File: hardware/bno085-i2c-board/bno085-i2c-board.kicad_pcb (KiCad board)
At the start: 2 copper layers, 9.5 x 15.5 mm, 8 parts, among them J1 Conn_01x06_Pin

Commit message: pcb
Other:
- board size 9.5 x 15.5 mm -> 9.5 x 15 mm
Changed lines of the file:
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@@
   (gr_arc (start 163.5 97) (mid 163.353553 97.353553) (end 163 97.5)
     (stroke (width 0.1) (type default)) (layer "Edge.Cuts"))
-  (gr_arc (start 163 82) (mid 163.353553 82.146447) (end 163.5 82.5)
+  (gr_arc (start 163 82.5) (mid 163.353553 82.646447) (end 163.5 83)
     (stroke (width 0.1) (type default)) (layer "Edge.Cuts"))
-  (gr_line (start 154 82.5) (end 154 97)
+  (gr_line (start 154 83) (end 154 97)
     (stroke (width 0.1) (type default)) (layer "Edge.Cuts"))
   (gr_arc (start 154.5 97.5) (mid 154.146447 97.353553) (end 154 97)
     (stroke (width 0.1) (type default)) (layer "Edge.Cuts"))
-  (gr_arc (start 154 82.5) (mid 154.146447 82.146447) (end 154.5 82)
+  (gr_arc (start 154 83) (mid 154.146447 82.646447) (end 154.5 82.5)
     (stroke (width 0.1) (type default)) (layer "Edge.Cuts"))
-  (gr_line (start 163 82) (end 154.5 82)
+  (gr_line (start 163 82.5) (end 154.5 82.5)
     (stroke (width 0.1) (type default)) (layer "Edge.Cuts"))
-  (gr_line (start 163.5 82.5) (end 163.5 97)
+  (gr_line (start 163.5 83) (end 163.5 97)
     (stroke (width 0.1) (type default)) (layer "Edge.Cuts"))
   (gr_line (start 163 97.5) (end 154.5 97.5)

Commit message: pcb
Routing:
- net GND: track 24.6 -> 41.8 mm
- net /H_SCL: track 13.1 -> 18.7 mm
- net +3.3V: track 21.9 -> 24.2 mm, vias 2 -> 3

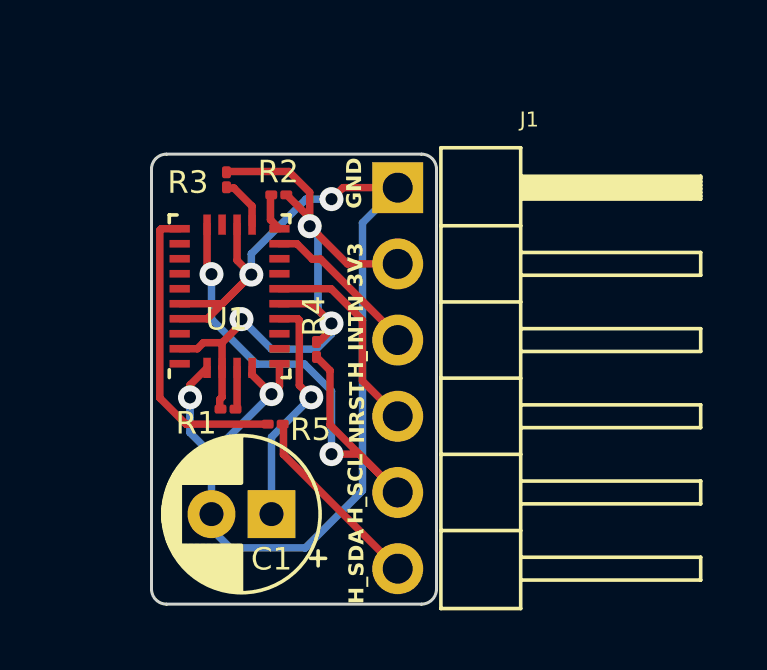
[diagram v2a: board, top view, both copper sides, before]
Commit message: new pcb resistors
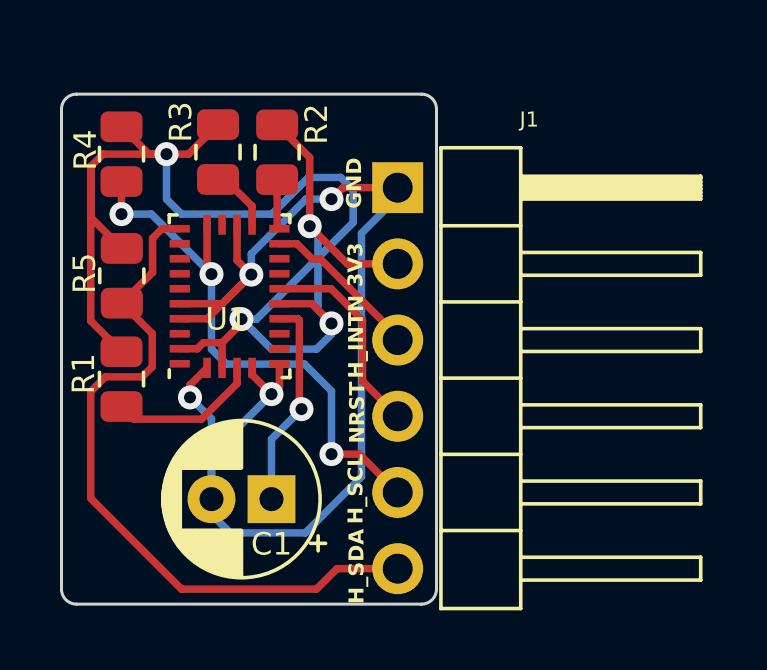
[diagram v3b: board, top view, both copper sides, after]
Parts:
- R1, R2, R3, R4, R5: footprint Resistor_SMD:R_01005_0402Metric -> Resistor_SMD:R_0805_2012Metric
- moved R4 9.20 mm to (153.0, 82.5)
- moved R5 7.11 mm to (153.0, 86.6), turned to 90 degrees
- moved R1 3.69 mm to (153.0, 90.0), turned to 90 degrees
- moved R2 1.42 mm to (158.2, 82.4), turned to -90 degrees
- moved R3 0.97 mm to (156.2, 82.4)
- moved C1 0.50 mm to (158.0, 94.0)
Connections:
- R5 pad 2: Net-(U1-H_SDA/H_MISO/TX) -> +3.3V
- U1 pad 20: Net-(U1-H_SDA/H_MISO/TX) -> /H_SDA
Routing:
- net +3.3V: track 24.2 -> 51.8 mm, vias 3 -> 4
- net /H_SDA: track 6.40 -> 23.9 mm
- net Net-(U1-H_SDA/H_MISO/TX): track 10.2 -> 0.00 mm
- net Net-(U1-BOOTN): track 1.39 -> 5.04 mm
- net Net-(U1-CAP): track 7.86 -> 7.09 mm
- net GND: track 41.8 -> 42.3 mm
- net /H_SCL: track 18.7 -> 18.5 mm, vias 2 -> 3
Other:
- board size 9.5 x 15 mm -> 12.5 x 17 mm

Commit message: pcb
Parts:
- moved J1 0.96 mm to (162.2, 82.7)
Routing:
- net GND: track 42.3 -> 44.0 mm
- net /NRST: track 6.89 -> 5.85 mm
- net +3.3V: track 51.8 -> 51.1 mm

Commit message: more pcb
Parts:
- moved J1 0.54 mm to (162.4, 82.1)
- moved C1 0.50 mm to (158.0, 93.5)
- moved R1 0.22 mm to (153.2, 90.0)
- moved R5 0.22 mm to (153.2, 86.6)
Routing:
- net /H_SDA: track 24.0 -> 21.2 mm
- net GND: track 44.0 -> 42.2 mm
- net +3.3V: track 51.1 -> 51.7 mm
- net Net-(U1-CAP): track 7.09 -> 6.59 mm
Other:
- board size 12.5 x 17 mm -> 12.5 x 16 mm

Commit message: pcb
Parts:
- moved R4 0.27 mm to (153.3, 82.5)
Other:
- board size 12.5 x 16 mm -> 12 x 16 mm
- board text added: "INTN"
- board text added: "SCL"
- board text added: "SDA"
- board text removed: "H_INTN"
- board text removed: "H_SCL"
- board text removed: "H_SDA"
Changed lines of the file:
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@@
   (net 21 "unconnected-(U1-XIN32-Pad27)")
   (footprint "Resistor_SMD:R_0805_2012Metric" (layer "F.Cu")
-    (at 153 82.5 -90)
+    (at 153.272899 82.49508 -90)
     (descr "Resistor SMD 0805 (2012 Metric), square (rectangular) end terminal, IPC_7351 nominal, (Body size source: IPC-SM-782 page 72, https://www.pcb-3d.com/wordpress/wp-content/uploads/ipc-sm-782a_amendment_1_and_2.pdf), generated with kicad-footprint-generator")
     (tags "resistor")
@@
     (property "ki_keywords" "R resistor")
     (attr smd)
-    (fp_text reference "R4" (at -0.137577 1.202034 90) (layer "F.SilkS")
+    (fp_text reference "R4" (at -0.005677 1.214987 90) (layer "F.SilkS")
         (effects (font (size 0.75 0.75) (thickness 0.12)))
     )
@@
     (property "ki_keywords" "R resistor")
     (attr smd)
-    (fp_text reference "R1" (at 0.181529 -1.261802 90) (layer "F.SilkS")
+    (fp_text reference "R1" (at -0.002481 -1.219655 90) (layer "F.SilkS")
         (effects (font (size 0.75 0.75) (thickness 0.12)))
     )
@@
     (property "ki_keywords" "R resistor")
     (attr smd)
-    (fp_text reference "R5" (at 0.084374 -1.24217 90) (layer "F.SilkS")
+    (fp_text reference "R5" (at 0.005114 -1.20685 90) (layer "F.SilkS")
         (effects (font (size 0.75 0.75) (thickness 0.12)))
     )
@@
     )
   )
-  (gr_line (start 151.5 96.5) (end 163 96.5)
+  (gr_line (start 152 96.5) (end 163 96.5)
     (stroke (width 0.1) (type default)) (layer "Edge.Cuts"))
-  (gr_arc (start 151.5 96.5) (mid 151.146447 96.353553) (end 151 96)
+  (gr_line (start 163 80.5) (end 152 80.5)
     (stroke (width 0.1) (type default)) (layer "Edge.Cuts"))
-  (gr_line (start 163 80.5) (end 151.5 80.5)
+  (gr_arc (start 151.5 81) (mid 151.646447 80.646447) (end 152 80.5)
     (stroke (width 0.1) (type default)) (layer "Edge.Cuts"))
   (gr_line (start 163.5 81) (end 163.5 96)
     (stroke (width 0.1) (type default)) (layer "Edge.Cuts"))
-  (gr_line (start 151 81) (end 151 96)
+  (gr_line (start 151.5 81) (end 151.5 96)
     (stroke (width 0.1) (type default)) (layer "Edge.Cuts"))
   (gr_arc (start 163.5 96) (mid 163.353553 96.353553) (end 163 96.5)
@@
   (gr_arc (start 163 80.5) (mid 163.353553 80.646447) (end 163.5 81)
     (stroke (width 0.1) (type default)) (layer "Edge.Cuts"))
-  (gr_arc (start 151 81) (mid 151.146447 80.646447) (end 151.5 80.5)
+  (gr_arc (start 152 96.5) (mid 151.646447 96.353553) (end 151.5 96)
     (stroke (width 0.1) (type default)) (layer "Edge.Cuts"))
-  (gr_text "3V3" (at 161.091404 86 90) (layer "F.SilkS")
+  (gr_text "3V3" (at 161.203323 85.357604 90) (layer "F.SilkS")
     (effects (font (size 0.5 0.5) (thickness 0.1) bold) (justify left bottom))
   )
-  (gr_text "H_INTN" (at 161.113727 89 90) (layer "F.SilkS")
+  (gr_text "INTN" (at 161.21745 88.154841 90) (layer "F.SilkS")
     (effects (font (size 0.5 0.5) (thickness 0.1) bold) (justify left bottom))
   )
-  (gr_text "H_SDA" (at 161.047872 96.5 90) (layer "F.SilkS")
+  (gr_text "SDA" (at 161.203323 95.600013 90) (layer "F.SilkS")
     (effects (font (size 0.5 0.5) (thickness 0.1) bold) (justify left bottom))
   )
-  (gr_text "GND" (at 161.046759 83.5 90) (layer "F.SilkS")
+  (gr_text "GND" (at 161.189195 82.941808 90) (layer "F.SilkS")
     (effects (font (size 0.5 0.5) (thickness 0.1) bold) (justify left bottom))
   )
-  (gr_text "NRST" (at 161.105288 91.248715 90) (layer "F.SilkS")
+  (gr_text "NRST" (at 161.189195 90.697784 90) (layer "F.SilkS")
     (effects (font (size 0.5 0.5) (thickness 0.1) bold) (justify left bottom))
   )
-  (gr_text "H_SCL" (at 161.087994 94.058983 90) (layer "F.SilkS")
+  (gr_text "SCL" (at 161.189195 92.986432 90) (layer "F.SilkS")
     (effects (font (size 0.5 0.5) (thickness 0.1) bold) (justify left bottom))
   )
   (dimension (type orthogonal) (layer "Cmts.User")
-    (pts (xy 152 80.5) (xy 152 96.5))
+    (pts (xy 153 80.5) (xy 153 96.5))
     (height -4)
     (orientation 1)
-    (gr_text "16.0000 mm" (at 146.85 88.5 90) (layer "Cmts.User")
+    (gr_text "16.0000 mm" (at 147.85 88.5 90) (layer "Cmts.User")
       (effects (font (size 1 1) (thickness 0.15)))
     )
@@
   )
   (dimension (type orthogonal) (layer "Cmts.User")
-    (pts (xy 151 94.5) (xy 163.5 94.088685))
+    (pts (xy 151.5 94.5) (xy 163.5 94.088685))
     (height 4.5)
     (orientation 0)
-    (gr_text "12.5000 mm" (at 157.25 97.85) (layer "Cmts.User")
+    (gr_text "12.0000 mm" (at 157.5 97.85) (layer "Cmts.User")
       (effects (font (size 1 1) (thickness 0.15)))
     )
@@
   (segment (start 160.190244 92.309756) (end 160 92.5) (width 0.25) (layer "F.Cu") (net 3))
   (segment (start 162.364959 92.309756) (end 160.190244 92.309756) (width 0.25) (layer "F.Cu") (net 3))
-  (segment (start 153 84.5) (end 153 83.4125) (width 0.25) (layer "F.Cu") (net 3))
-  (via (at 153 84.5) (size 0.8) (drill 0.4) (layers "F.Cu" "B.Cu") (net 3))
+  (segment (start 153.295609 84.5) (end 153.272899 84.47729) (width 0.25) (layer "F.Cu") (net 3))
+  (segment (start 153.272899 84.47729) (end 153.272899 83.40758) (width 0.25) (layer "F.Cu") (net 3))
+  (via (at 153.295609 84.5) (size 0.8) (drill 0.4) (layers "F.Cu" "B.Cu") (net 3))
   (via (at 160 92.5) (size 0.8) (drill 0.4) (layers "F.Cu" "B.Cu") (net 3))
   (via (at 156 86.5) (size 0.8) (drill 0.4) (layers "F.Cu" "B.Cu") (net 3))
   (segment (start 156.5 89.5) (end 156 89) (width 0.25) (layer "B.Cu") (net 3))
-  (segment (start 153 84.5) (end 154 84.5) (width 0.25) (layer "B.Cu") (net 3))
   (segment (start 160 92.5) (end 160 90.396539) (width 0.25) (layer "B.Cu") (net 3))
-  (segment (start 154 84.5) (end 156 86.5) (width 0.25) (layer "B.Cu") (net 3))
+  (segment (start 153.295609 84.5) (end 154 84.5) (width 0.25) (layer "B.Cu") (net 3))
   (segment (start 159.103461 89.5) (end 156.5 89.5) (width 0.25) (layer "B.Cu") (net 3))
   (segment (start 160 90.396539) (end 159.103461 89.5) (width 0.25) (layer "B.Cu") (net 3))
+  (segment (start 154 84.5) (end 156 86.5) (width 0.25) (layer "B.Cu") (net 3))
   (segment (start 156 89) (end 156 86.5) (width 0.25) (layer "B.Cu") (net 3))
   (segment (start 154.2775 86.419633) (end 153.230697 87.466436) (width 0.25) (layer "F.Cu") (net 4))
@@
   (segment (start 154.94 88.9875) (end 155.5275 88.9875) (width 0.25) (layer "F.Cu") (net 7))
   (segment (start 160 88.237501) (end 160.082645 88.320146) (width 0.25) (layer "F.Cu") (net 7))
+  (segment (start 153.272899 81.58258) (end 153.58258 81.58258) (width 0.25) (layer "F.Cu") (net 7))
   (segment (start 153.220792 89.085767) (end 152.998267 89.085767) (width 0.25) (layer "F.Cu") (net 7))
   (segment (start 155.7295 88.7855) (end 156.3525 88.7855) (width 0.25) (layer "F.Cu") (net 7))
@@
   (segment (start 160 88.142984) (end 159.344516 87.4875) (width 0.25) (layer "F.Cu") (net 7))
   (segment (start 155.235224 82.5) (end 156.216632 81.518592) (width 0.25) (layer "F.Cu") (net 7))
+  (segment (start 153.58258 81.58258) (end 154.5 82.5) (width 0.25) (layer "F.Cu") (net 7))
   (segment (start 160 88.142984) (end 160 88.3393) (width 0.25) (layer "F.Cu") (net 7))
   (segment (start 152.998267 89.085767) (end 151.975 88.0625) (width 0.25) (layer "F.Cu") (net 7))
@@
   (segment (start 151.975 82.911827) (end 151.975 88.0625) (width 0.25) (layer "F.Cu") (net 7))
   (segment (start 162.364959 84.689756) (end 162.152778 84.901937) (width 0.25) (layer "F.Cu") (net 7))
-  (segment (start 154.5 82.5) (end 153.9125 82.5) (width 0.25) (layer "F.Cu") (net 7))
   (segment (start 162.152778 84.901937) (end 159.273449 84.901937) (width 0.25) (layer "F.Cu") (net 7))
   (segment (start 151.975 82.911827) (end 151.975 84.608089) (width 0.25) (layer "F.Cu") (net 7))
@@
   (segment (start 154.5 82.5) (end 155.235224 82.5) (width 0.25) (layer "F.Cu") (net 7))
   (segment (start 153.008347 85.641436) (end 151.975 84.608089) (width 0.25) (layer "F.Cu") (net 7))
-  (segment (start 153.9125 82.5) (end 153 81.5875) (width 0.25) (layer "F.Cu") (net 7))
   (via (at 159.273449 84.901937) (size 0.8) (drill 0.4) (layers "F.Cu" "B.Cu") (net 7))
   (via (at 157 88) (size 0.8) (drill 0.4) (layers "F.Cu" "B.Cu") (net 7))

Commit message: new board
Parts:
- C1: footprint Capacitor_THT:CP_Radial_D5.0mm_P2.00mm -> Capacitor_SMD:CP_Elec_4x3.9
- moved C1 1.12 mm to (157.0, 93.0)
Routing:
- net /H_SDA: track 21.2 -> 24.8 mm
- net GND: track 42.2 -> 44.2 mm, vias 4 -> 5
- net /H_SCL: track 18.0 -> 16.9 mm
- net Net-(U1-CAP): track 6.59 -> 5.99 mm, vias 1 -> 0
